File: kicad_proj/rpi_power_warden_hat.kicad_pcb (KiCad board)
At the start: 2 copper layers, 65 x 56.5 mm, 77 parts, among them J1 54-00164, J2 54-00164, J3 54-00003, J4 Raspberry Pi SMT connector, J5 Conn_01x02, J6 Conn_01x04, J7 Conn_01x04, Q1 DMG2305UX-7, Q2 DMG2305UX-7, U1 INA260, U10 SN74AHC1G08DBVR, U2 INA260, U3 CAT24C32WI-GT3, U4 TPS563200, U5 DMMT5401-7-F, U6 TPS563200, U7 DMMT5401-7-F, U8 TPS22810DBVR, U9 SN74AHC1G08DBVR

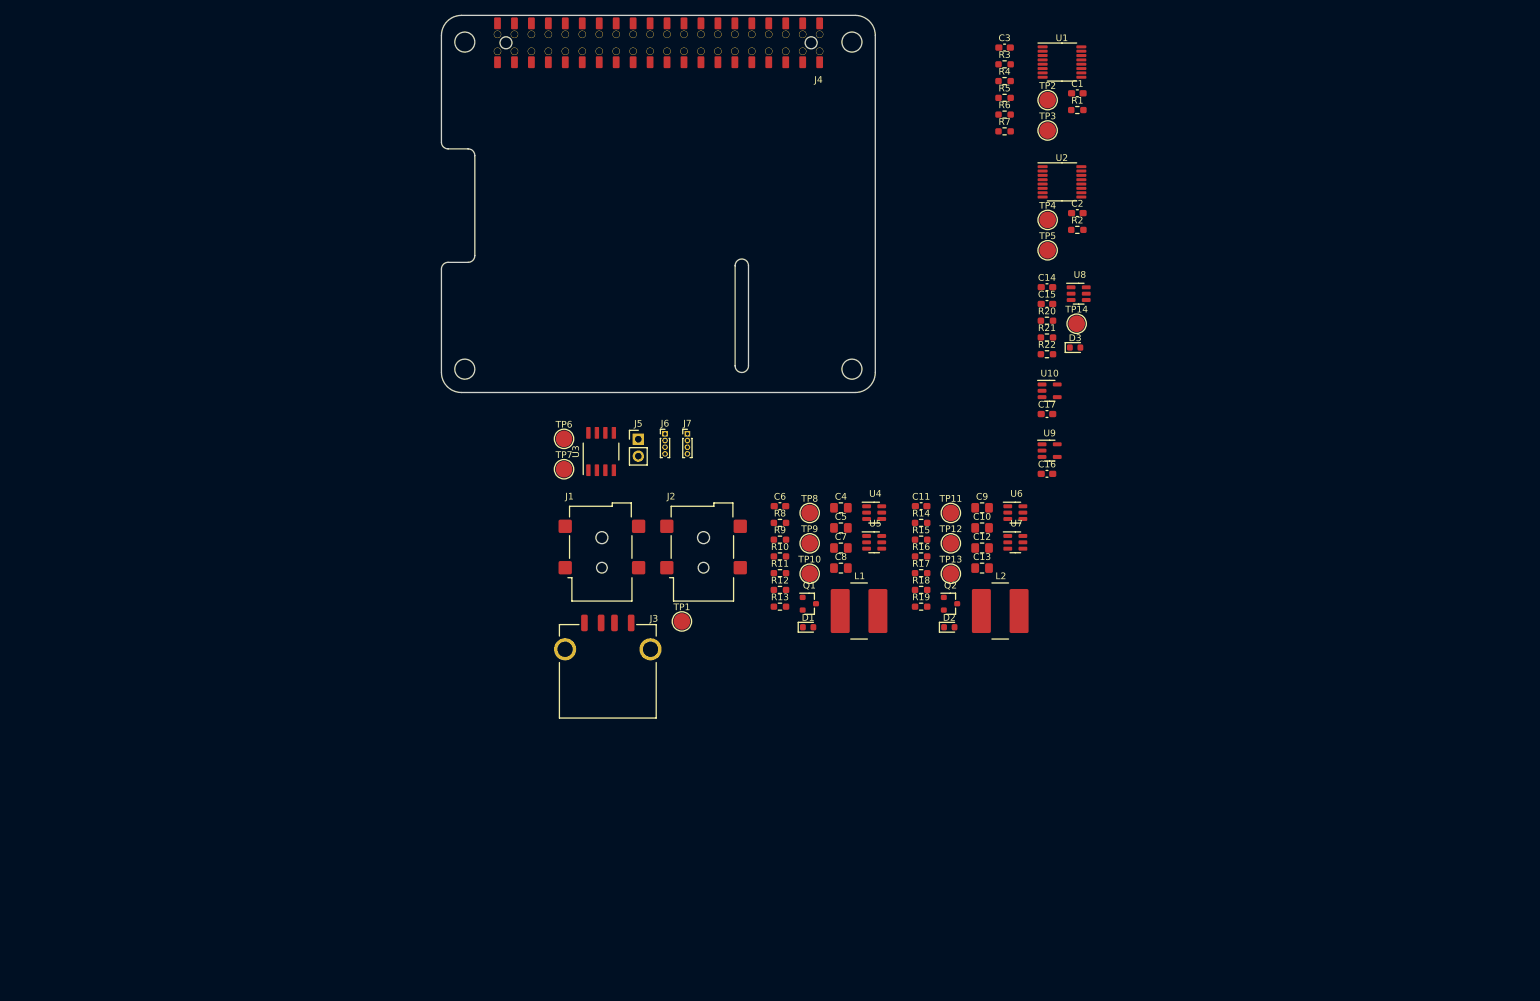
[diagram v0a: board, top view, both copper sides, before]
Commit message: loaded jlcpcb design constraints
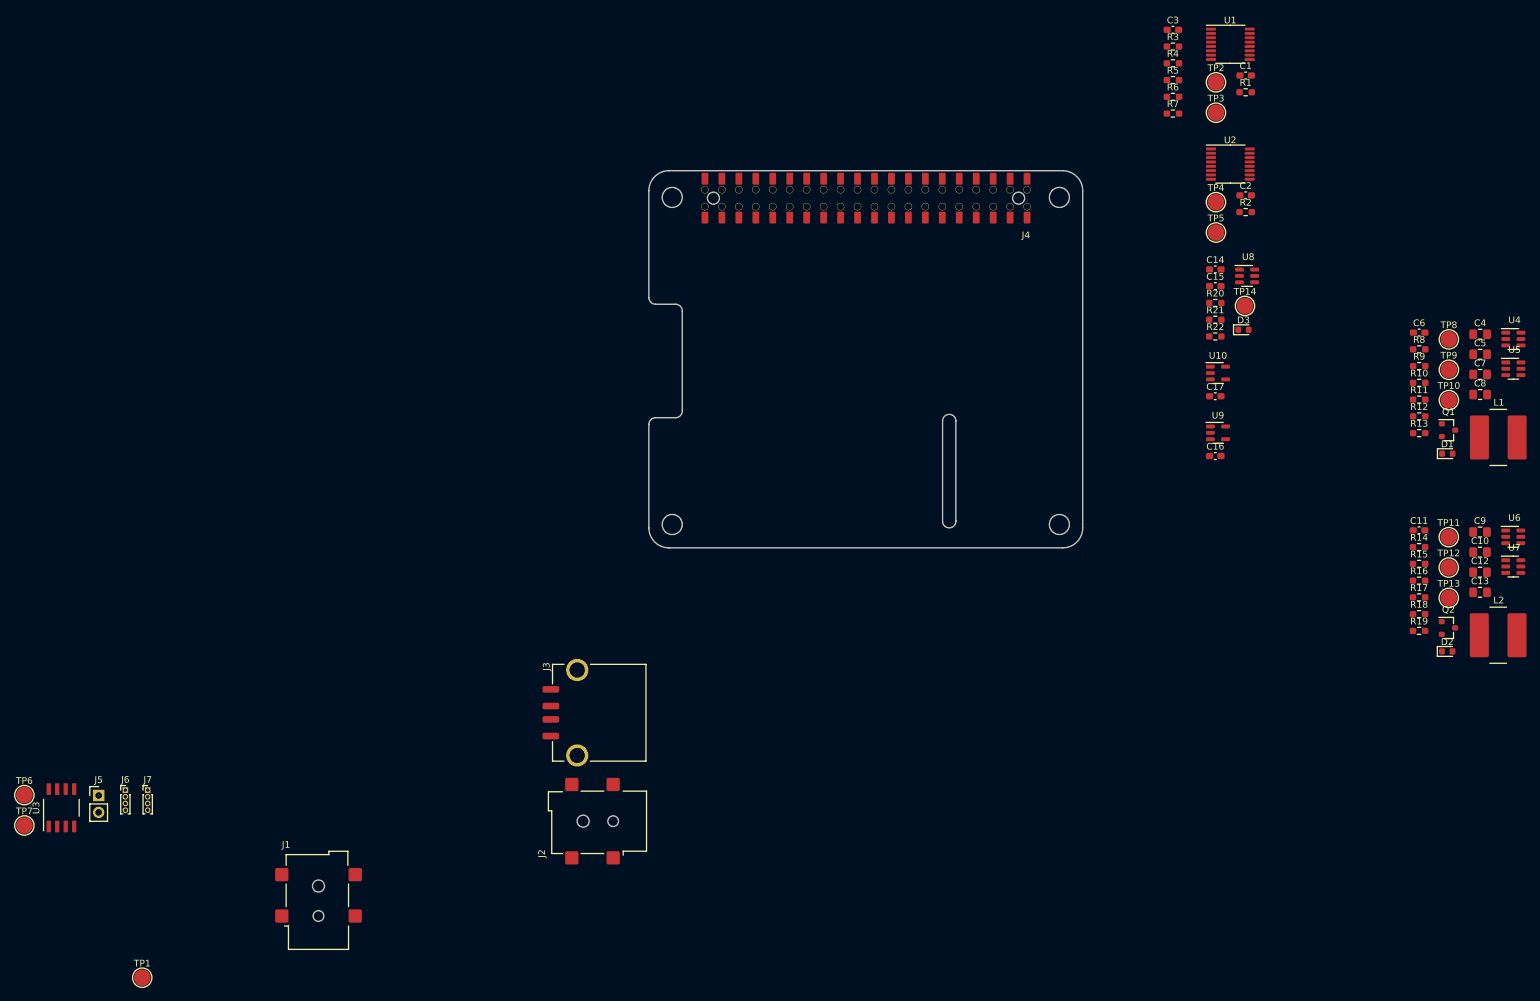
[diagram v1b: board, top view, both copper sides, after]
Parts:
- moved TP10 99.2 mm to (246.7, 104.2)
- moved TP8 99.2 mm to (246.7, 95.1)
- moved C4 99.2 mm to (251.4, 94.3)
- moved C5 99.2 mm to (251.4, 97.3)
- moved C6 99.2 mm to (242.3, 94.1)
- moved C7 99.2 mm to (251.4, 100.3)
- moved C8 99.2 mm to (251.4, 103.3)
- moved D1 99.2 mm to (246.5, 112.2)
- moved L1 99.2 mm to (254.1, 109.8)
- moved Q1 99.2 mm to (246.7, 108.7)
- moved R10 99.2 mm to (242.3, 101.6)
- moved R11 99.2 mm to (242.3, 104.1)
- moved R12 99.2 mm to (242.3, 106.6)
- moved R13 99.2 mm to (242.3, 109.1)
- moved R8 99.2 mm to (242.3, 96.6)
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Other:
- copper layers 2 -> 4

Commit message: progress a bit with the placement an replace 5 v buck converter L for a smaller one
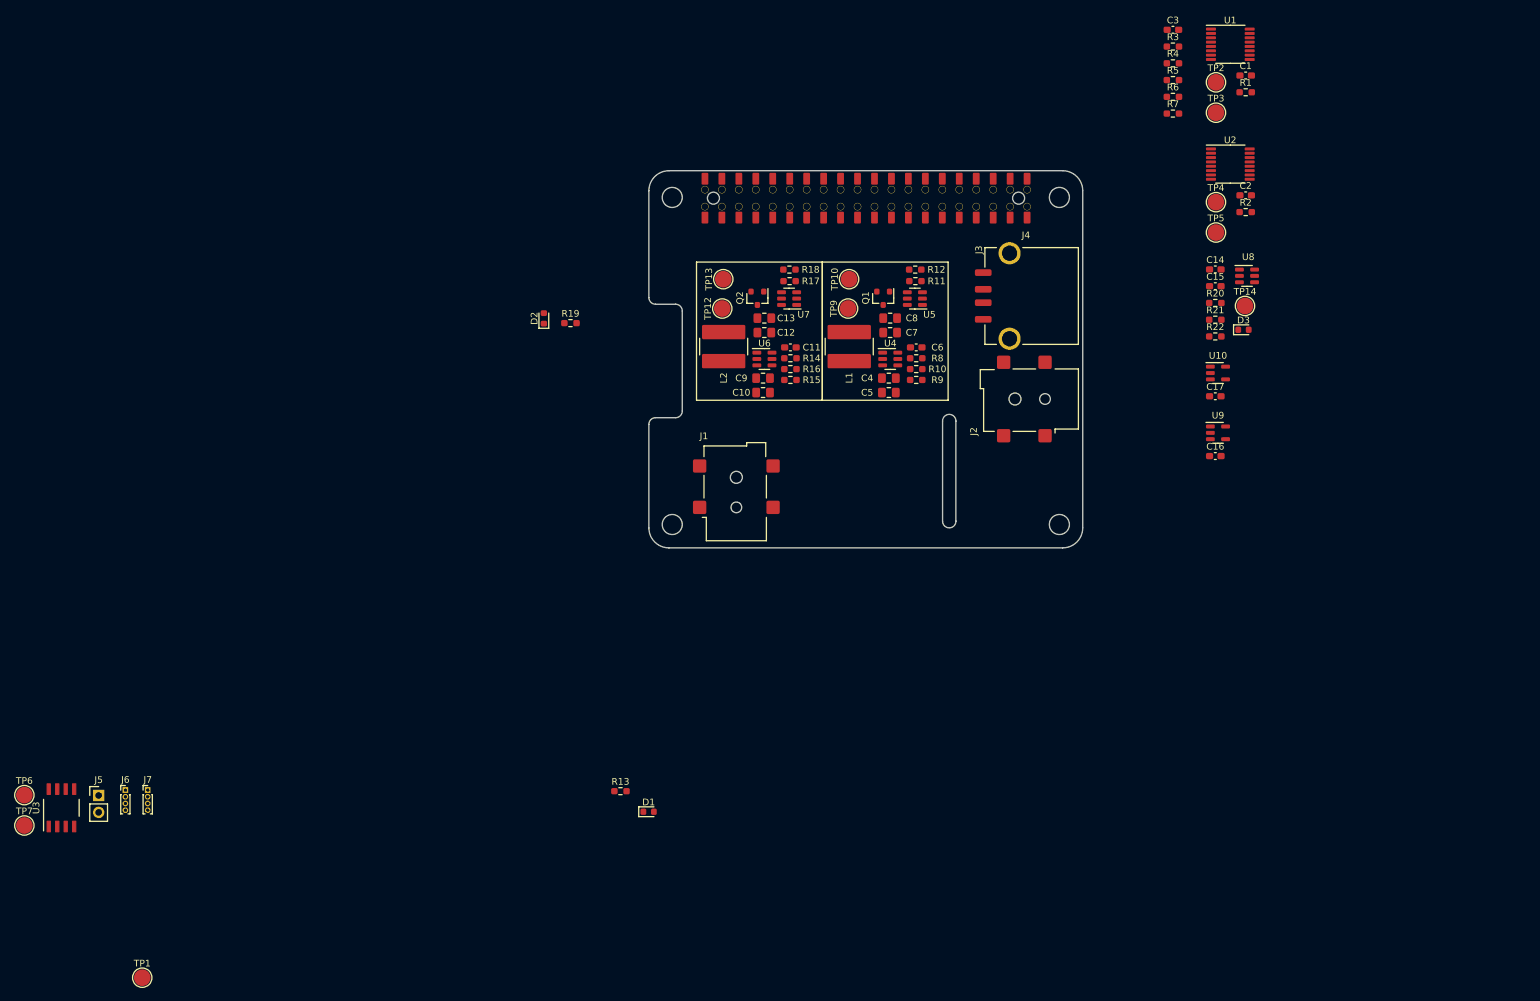
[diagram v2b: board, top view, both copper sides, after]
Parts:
- removed TP11, TP8: TestPoint, TestPoint:TestPoint_Pad_D2.5mm
- L1, L2: footprint rpi_power_warden_hat:L_8040_8x8x4mm -> rpi_power_warden_hat:L_6045_6x6x4mm
- moved D2 144.2 mm to (111.2, 91.9), turned to 90 degrees
- moved R19 135.2 mm to (115.2, 92.6)
- moved D1 131.1 mm to (126.9, 165.8)
- moved R13 131.1 mm to (122.6, 162.8)
- moved L2 123.8 mm to (138.1, 96.2), turned to 90 degrees
- moved TP13 118.7 mm to (138.0, 86.1), turned to 90 degrees
- moved U7 115.7 mm to (147.9, 89.0), turned to 180 degrees
- moved TP12 115.5 mm to (137.9, 90.5), turned to 90 degrees
- moved U6 115.3 mm to (144.2, 98.0)
- moved C13 114.8 mm to (144.2, 91.9)
- moved Q2 114.7 mm to (143.2, 88.9), turned to -90 degrees
- moved C12 113.1 mm to (144.2, 94.1)
- moved C10 110.0 mm to (144.0, 103.0)
- moved C9 109.9 mm to (144.0, 100.9)
- moved R18 107.5 mm to (148.0, 84.6), turned to 180 degrees
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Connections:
- net /rpi/CE0_SPI0/GPIO08 renamed /rpi/CE0_SPI0/GPIO08_1
- net /rpi/GPIO12/PWM0_1 renamed /rpi/GPIO12/PWM0
- net /rpi/GPIO13/PWM1 renamed /rpi/GPIO13/PWM1_1
- net /rpi/GPIO15/UART_RXD_1 renamed /rpi/GPIO15/UART_RXD
- net /rpi/GPIO16/SP1_CE2_1 renamed /rpi/GPIO16/SP1_CE2
- net /rpi/GPIO18/SPI1_CE0 renamed /rpi/GPIO18/SPI1_CE0_1
- net /rpi/GPIO19/SPI1_MISO_1 renamed /rpi/GPIO19/SPI1_MISO
- net /rpi/GPIO20/SPI1_MOSI_1 renamed /rpi/GPIO20/SPI1_MOSI
- net /rpi/GPIO21/SPI1_CLK renamed /rpi/GPIO21/SPI1_CLK_1
- net /rpi/GPIO22/SDIO_CLK_1 renamed /rpi/GPIO22/SDIO_CLK
- net /rpi/GPIO25/SDIO_DAT1_1 renamed /rpi/GPIO25/SDIO_DAT1
- net /rpi/GPIO26/SDIO_DAT2_1 renamed /rpi/GPIO26/SDIO_DAT2
- net /rpi/MOSI_SPI0/GPIO10_1 renamed /rpi/MOSI_SPI0/GPIO10

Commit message: finish placement
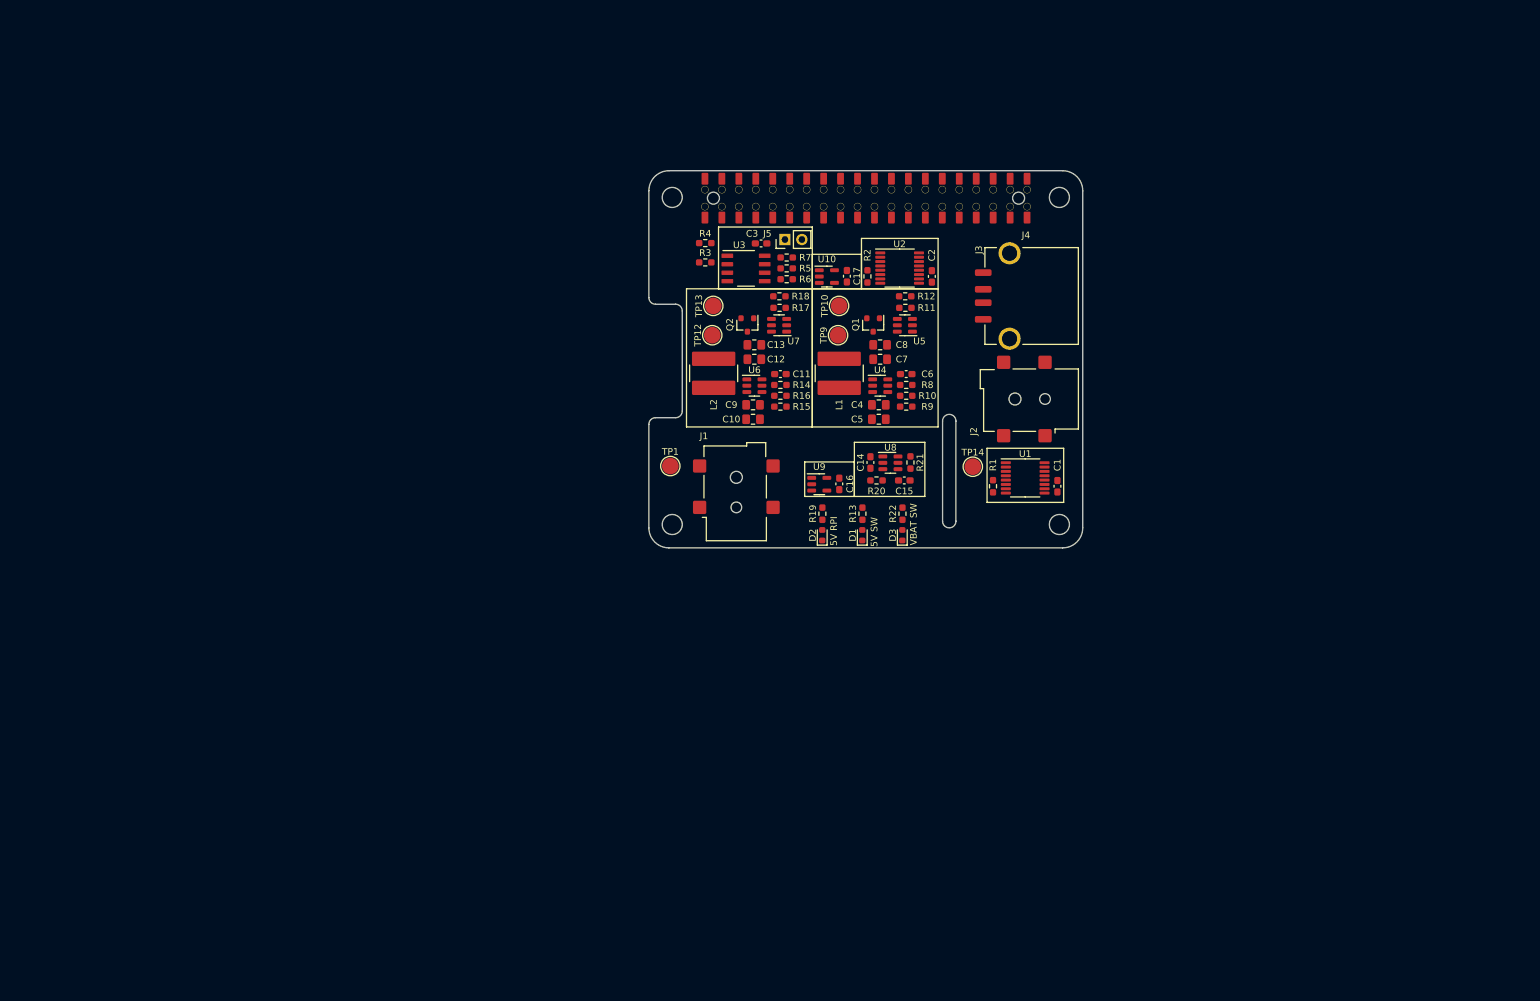
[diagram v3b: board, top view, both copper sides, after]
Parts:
- removed J6, J7: Conn_01x04, Connector_PinHeader_1.00mm:PinHeader_1x04_P1.00mm_Vertical
- removed TP2, TP3, TP4, TP5, TP6, TP7: TestPoint, TestPoint:TestPoint_Pad_D2.5mm
- moved J5 132.3 mm to (147.3, 80.1), turned to 90 degrees
- moved U3 130.6 mm to (141.4, 84.4), turned to -90 degrees
- moved TP1 110.2 mm to (130.1, 114.1)
- moved R3 77.2 mm to (135.3, 83.6)
- moved R4 75.1 mm to (135.3, 80.7)
- moved U1 71.9 mm to (183.3, 115.8)
- moved R1 70.1 mm to (178.5, 117.1), turned to 90 degrees
- moved C3 69.5 mm to (143.7, 80.7), turned to 180 degrees
- moved C1 67.7 mm to (188.1, 117.1), turned to 90 degrees
- moved R5 64.4 mm to (147.5, 84.4), turned to 180 degrees
- moved R6 64.0 mm to (147.5, 86.1)
- moved R7 61.8 mm to (147.5, 82.8), turned to 180 degrees
- moved U10 60.3 mm to (153.6, 85.7)
- moved U8 60.3 mm to (163.1, 113.6)
- moved U9 60.2 mm to (152.4, 116.8)
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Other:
- board text added: "5V RPI"
- board text added: "5V SW"
- board text added: "VBAT SW"

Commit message: progress with layout
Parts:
- moved R17 7.01 mm to (149.7, 96.6)
- moved R11 7.01 mm to (168.5, 96.6)
- moved R4 4.46 mm to (136.4, 85.0), turned to 90 degrees
- moved R12 4.27 mm to (168.6, 91.3)
- moved R18 4.27 mm to (149.8, 91.3)
- moved R3 2.76 mm to (136.4, 81.0), turned to 90 degrees
- moved R16 2.64 mm to (146.9, 106.2)
- moved R10 2.64 mm to (165.7, 106.2)
- moved U7 1.64 mm to (147.7, 94.0)
- moved U5 1.64 mm to (166.5, 94.0)
- moved C14 1.30 mm to (160.1, 112.2)
- moved R20 1.30 mm to (161.0, 114.9)
- moved R21 1.30 mm to (166.1, 112.2)
- moved U8 1.30 mm to (163.1, 112.3)
- moved U9 1.30 mm to (152.5, 115.5)
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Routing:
- net /and_5v/Y: track 0.00 -> 23.4 mm, vias 0 -> 2
- net Net-(U6-SW): track 0.00 -> 21.2 mm, vias 0 -> 2
- net Net-(U4-SW): track 0.00 -> 21.0 mm, vias 0 -> 2
- net Net-(Q1-D): track 0.00 -> 18.7 mm, vias 0 -> 2
- net Net-(Q2-D): track 0.00 -> 17.0 mm, vias 0 -> 2
- net /+VBAT: track 0.00 -> 13.6 mm, vias 0 -> 2
- net Net-(U5-B1): track 0.00 -> 7.65 mm
- net Net-(Q1-G): track 0.00 -> 7.59 mm, vias 0 -> 2
- net Net-(Q2-G): track 0.00 -> 7.58 mm, vias 0 -> 2
- net Net-(U7-B1): track 0.00 -> 7.38 mm
- net /rpi/+5V_RPI: track 0.00 -> 6.35 mm
- net /current_sensor_5V/+VCC_IN: track 0.00 -> 6.19 mm
- net Net-(U6-VFB): track 0.00 -> 4.16 mm
- net Net-(U4-VFB): track 0.00 -> 3.74 mm
- net Net-(U6-VBST): track 0.00 -> 2.56 mm
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- added copper zone on F.Cu, net /+VBAT
- added copper zone on F.Cu, net /current_sensor_5V/+VCC_IN
- added copper zone on F.Cu, net /rpi/+5V_RPI
- added copper zone on B.Cu, net GND
- added copper zone on F.Cu, net GND
- added copper zone on In1.Cu, net GND
- added copper zone on In2.Cu, net GND
- added copper zone on F.Cu, net Net-(Q1-D)
- added copper zone on F.Cu, net Net-(Q2-D)
